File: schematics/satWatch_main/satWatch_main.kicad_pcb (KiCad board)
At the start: 2 copper layers, 40 x 30 mm, 117 parts, among them J1 PogoPins_02x17_Data, J2 UJ20-C-H-G-MSMT-2B-P16-TR, J5 Pogo_02x03_Power, Q1 FS8205, Q2 BSS138, Q3 DMP1045U, Q4 BSS138, SW1 B3U-1000P, SW2 B3U-1000P, SW3 B3U-1000P, SW4 B3U-1000P, SW5 B3U-1000P, U1 ESP32-S3-MINI-1, U10 VEMD8080, U11 VEMD8080, U12 BNO085, U2 MAX86141, U3 MAX32664GTGC, U4 NCP186AMX330TAG, U5 DS3231MZ, U6 MIC5365-1.8YC5, U7 PAM2401SCADJ, U8 TP4056-42-ESOP8, U9 DW01A, Y1 32.768kHz, Y2 32.768Hz

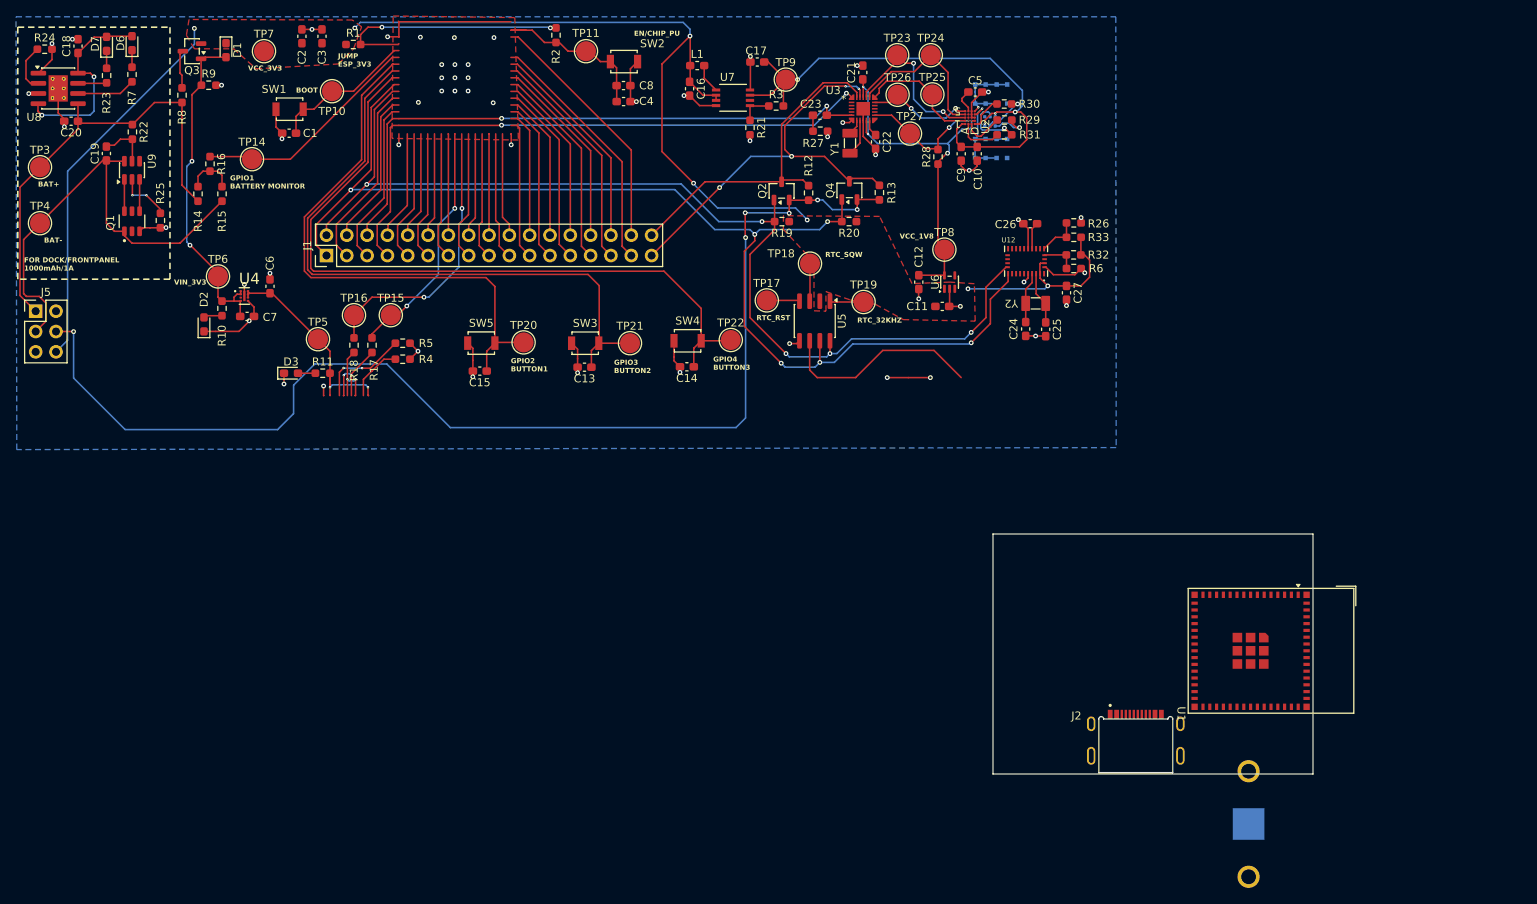
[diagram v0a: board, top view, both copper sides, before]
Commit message: v0.6
Began  layout work on watch-sized PCB. Backup of in-progress
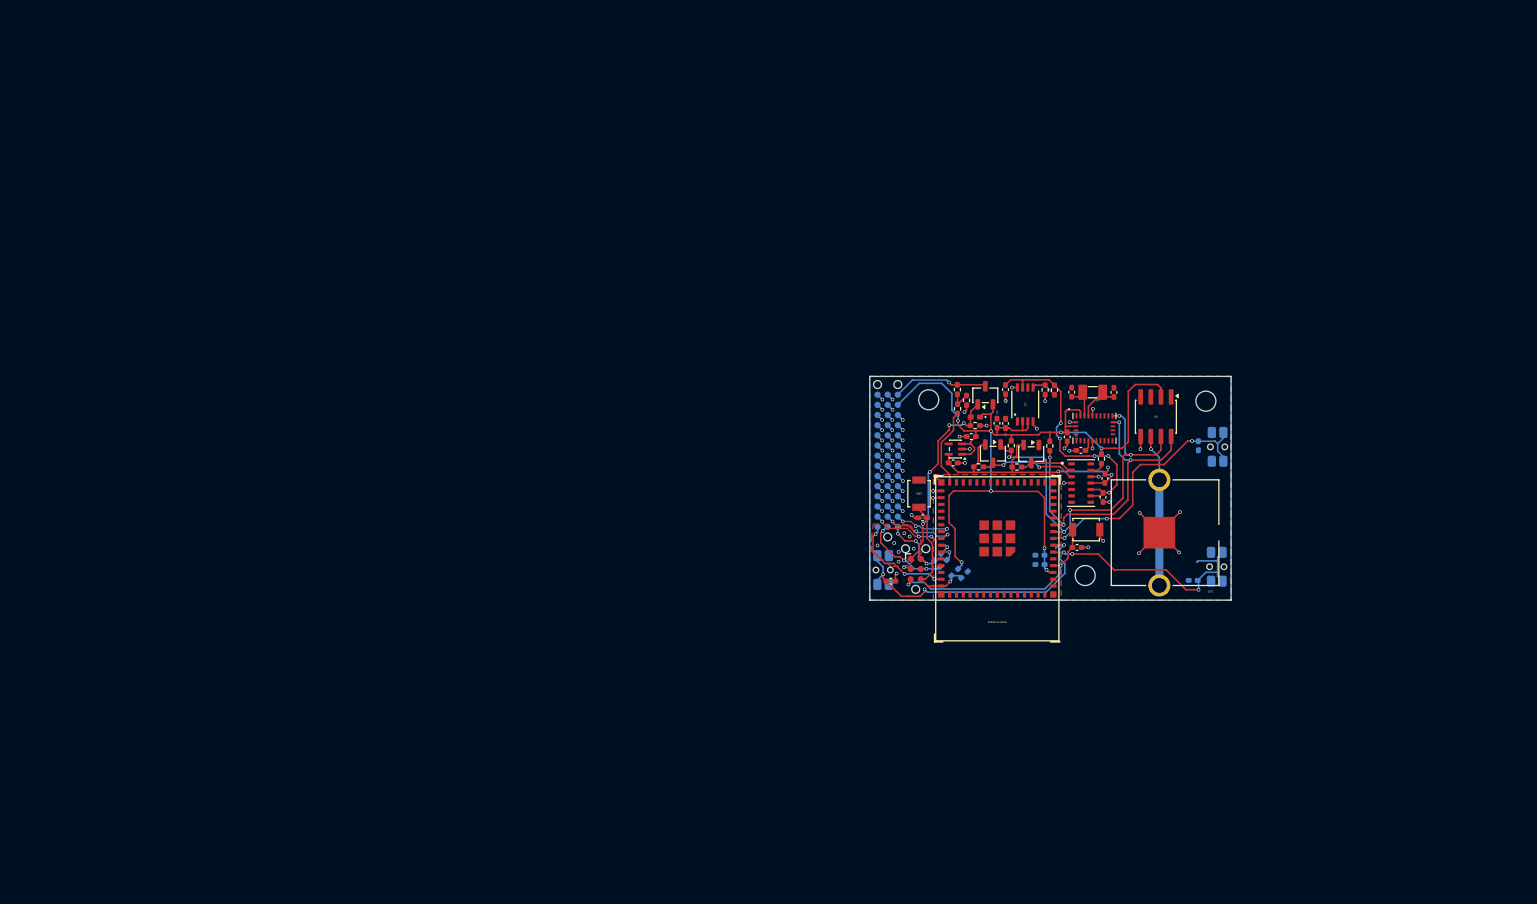
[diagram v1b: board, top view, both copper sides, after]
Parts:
- removed BT3: 2895 (CR1220 Holder), footprint:BAT_2895
- removed C19, C26, C27: 0.1uF, Capacitor_SMD:C_0603_1608Metric_Pad1.08x0.95mm_HandSolder
- removed C20: 10uF, Capacitor_SMD:C_0603_1608Metric_Pad1.08x0.95mm_HandSolder
- removed C21, C22, C23: 1uF, Capacitor_SMD:C_0603_1608Metric_Pad1.08x0.95mm_HandSolder
- removed C24, C25: 22pF, Capacitor_SMD:C_0603_1608Metric_Pad1.08x0.95mm_HandSolder
- removed D2: RED, LED_SMD:LED_0603_1608Metric_Pad1.05x0.95mm_HandSolder
- removed D3: YELLOW, LED_SMD:LED_0603_1608Metric_Pad1.05x0.95mm_HandSolder
- removed D6: DONE, LED_SMD:LED_0603_1608Metric_Pad1.05x0.95mm_HandSolder
- removed D7: CHRG, LED_SMD:LED_0603_1608Metric_Pad1.05x0.95mm_HandSolder
- removed J5: Pogo_02x03_Power, Connector_PinHeader_2.54mm:PinHeader_2x03_P2.54mm_Vertical
- removed LED1: SFH 7016, footprint:SFH7016
- removed Q4: BSS138, Package_TO_SOT_SMD:SOT-23-3
- removed R15: 220K, Resistor_SMD:R_0603_1608Metric_Pad0.98x0.95mm_HandSolder
- removed R16, R29, R30, R31, R32, R33: 0, Resistor_SMD:R_0603_1608Metric_Pad0.98x0.95mm_HandSolder
- removed R17, R18: 22, Resistor_SMD:R_0603_1608Metric_Pad0.98x0.95mm_HandSolder
- removed R19, R20: 2.2K, Resistor_SMD:R_0603_1608Metric_Pad0.98x0.95mm_HandSolder
- removed R21, R28: 100K, Resistor_SMD:R_0603_1608Metric_Pad0.98x0.95mm_HandSolder
- removed R22: 100, Resistor_SMD:R_0603_1608Metric_Pad0.98x0.95mm_HandSolder
- removed R23, R25: 1K, Resistor_SMD:R_0603_1608Metric_Pad0.98x0.95mm_HandSolder
- removed R24: 1.2k, Resistor_SMD:R_0603_1608Metric_Pad0.98x0.95mm_HandSolder
- removed R26: 10K, Resistor_SMD:R_0603_1608Metric_Pad0.98x0.95mm_HandSolder
- removed R27: 10, Resistor_SMD:R_0603_1608Metric_Pad0.98x0.95mm_HandSolder
- removed TP10: BOOT, TestPoint:TestPoint_Pad_D2.5mm
- removed TP11: EN, TestPoint:TestPoint_Pad_D2.5mm
- removed TP14: BAT_MONITOR, TestPoint:TestPoint_Pad_D2.5mm
- removed TP15: D-, TestPoint:TestPoint_Pad_D2.5mm
- removed TP16: D+, TestPoint:TestPoint_Pad_D2.5mm
- removed TP17: RTC_RST, TestPoint:TestPoint_Pad_D2.5mm
- removed TP18: SQW, TestPoint:TestPoint_Pad_D2.5mm
- removed TP19: 32KHZ, TestPoint:TestPoint_Pad_D2.5mm
- removed TP20: BUTTON1, TestPoint:TestPoint_Pad_D2.5mm
- removed TP21: BUTTON2, TestPoint:TestPoint_Pad_D2.5mm
- removed TP22: BUTTON3, TestPoint:TestPoint_Pad_D2.5mm
- removed TP23: PPG_MISO, TestPoint:TestPoint_Pad_D2.5mm
- removed TP24: PPG_MOSI, TestPoint:TestPoint_Pad_D2.5mm
- removed TP25: PPG_SCK, TestPoint:TestPoint_Pad_D2.5mm
- removed TP26: PPG_CSB, TestPoint:TestPoint_Pad_D2.5mm
- removed TP27: PPG_INT, TestPoint:TestPoint_Pad_D2.5mm
- removed TP3: BAT+, TestPoint:TestPoint_Pad_D2.5mm
- removed TP4: BAT-, TestPoint:TestPoint_Pad_D2.5mm
- removed TP5: VUSB_5V, TestPoint:TestPoint_Pad_D2.5mm
- removed TP6: VIN_3V3, TestPoint:TestPoint_Pad_D2.5mm
- removed TP7: VCC_3V3, TestPoint:TestPoint_Pad_D2.5mm
- removed TP8: VCC_1V8, TestPoint:TestPoint_Pad_D2.5mm
- removed TP9: IC_5V, TestPoint:TestPoint_Pad_D2.5mm
- removed U10, U11: VEMD8080, footprint:VEMD8080
- removed U12: BNO085, footprint:IC_BNO085
- removed U7: PAM2401SCADJ, footprint:MSOP8_DIO
- removed U8: TP4056-42-ESOP8, Package_SO:SOIC-8-1EP_3.9x4.9mm_P1.27mm_EP2.41x3.3mm_ThermalVias
- removed U9: DW01A, Package_TO_SOT_SMD:SOT-23-6
- removed Y2: 32.768Hz, footprint:ABS07-32.768KHZ-T
- added BT1: 2895 (CR1220 Holder), footprint:BAT_2895, F.Cu at (163.2, 95.7)
- added H1: MountingHole, MountingHole:MountingHole_2.5mm, F.Cu at (134.4, 79.1)
- added H2: MountingHole, MountingHole:MountingHole_2.5mm, F.Cu at (169.0, 79.3)
- added H3: MountingHole, MountingHole:MountingHole_2.5mm, F.Cu at (153.9, 101.1)
- C1: value 0.1uF/50V(10%) -> 1uF; footprint Capacitor_SMD:C_0603_1608Metric_Pad1.08x0.95mm_HandSolder -> Capacitor_SMD:C_0402_1005Metric_Pad0.74x0.62mm_HandSolder
- C10: value 0.1uF -> 10uF; footprint Capacitor_SMD:C_0603_1608Metric_Pad1.08x0.95mm_HandSolder -> Capacitor_SMD:C_0402_1005Metric_Pad0.74x0.62mm_HandSolder
- C11: value 1uF -> 0.1uF/50V(10%); footprint Capacitor_SMD:C_0603_1608Metric_Pad1.08x0.95mm_HandSolder -> Capacitor_SMD:C_0402_1005Metric_Pad0.74x0.62mm_HandSolder; moved to B.Cu
- C12, C5: value 1uF -> 0.1uF/50V(10%); footprint Capacitor_SMD:C_0603_1608Metric_Pad1.08x0.95mm_HandSolder -> Capacitor_SMD:C_0402_1005Metric_Pad0.74x0.62mm_HandSolder
- C13, C15: value 0.1uF/50V(10%) -> 0.1uF; footprint Capacitor_SMD:C_0603_1608Metric_Pad1.08x0.95mm_HandSolder -> Capacitor_SMD:C_0402_1005Metric_Pad0.74x0.62mm_HandSolder
- C14: footprint Capacitor_SMD:C_0603_1608Metric_Pad1.08x0.95mm_HandSolder -> Capacitor_SMD:C_0402_1005Metric_Pad0.74x0.62mm_HandSolder; moved to B.Cu
- C16: value 10uF -> 0.1uF; footprint Capacitor_SMD:C_0603_1608Metric_Pad1.08x0.95mm_HandSolder -> Capacitor_SMD:C_0402_1005Metric_Pad0.74x0.62mm_HandSolder
- C17: value 22uF -> 22pF; footprint Capacitor_SMD:C_0603_1608Metric_Pad1.08x0.95mm_HandSolder -> Capacitor_SMD:C_0402_1005Metric_Pad0.74x0.62mm_HandSolder
- C18: value 0.1uF -> 22pF; footprint Capacitor_SMD:C_0603_1608Metric_Pad1.08x0.95mm_HandSolder -> Capacitor_SMD:C_0402_1005Metric_Pad0.74x0.62mm_HandSolder
- C2: value 1uF/16V(10%) -> 10uF; footprint Capacitor_SMD:C_0603_1608Metric_Pad1.08x0.95mm_HandSolder -> Capacitor_SMD:C_0402_1005Metric_Pad0.74x0.62mm_HandSolder
- C3: value 10uF/16V(10%) -> 0.1uF/50V(10%); footprint Capacitor_SMD:C_0603_1608Metric_Pad1.08x0.95mm_HandSolder -> Capacitor_SMD:C_0402_1005Metric_Pad0.74x0.62mm_HandSolder
- C4: value 1uF/16V(10%) -> 1uF; footprint Capacitor_SMD:C_0603_1608Metric_Pad1.08x0.95mm_HandSolder -> Capacitor_SMD:C_0402_1005Metric_Pad0.74x0.62mm_HandSolder
- C6: value 1uF -> 22uF; footprint Capacitor_SMD:C_0603_1608Metric_Pad1.08x0.95mm_HandSolder -> Capacitor_SMD:C_0402_1005Metric_Pad0.74x0.62mm_HandSolder
- C7: value 1uF -> 1uF/16V(10%); footprint Capacitor_SMD:C_0603_1608Metric_Pad1.08x0.95mm_HandSolder -> Capacitor_SMD:C_0402_1005Metric_Pad0.74x0.62mm_HandSolder; moved to B.Cu
- C8: value 0.1uF/50V(10%) -> 1uF/16V(10%); footprint Capacitor_SMD:C_0603_1608Metric_Pad1.08x0.95mm_HandSolder -> Capacitor_SMD:C_0402_1005Metric_Pad0.74x0.62mm_HandSolder; moved to B.Cu
- C9: value 10uF -> 10uF/16V(10%); footprint Capacitor_SMD:C_0603_1608Metric_Pad1.08x0.95mm_HandSolder -> Capacitor_SMD:C_0402_1005Metric_Pad0.74x0.62mm_HandSolder; moved to B.Cu
- D1: footprint Diode_SMD:D_0603_1608Metric_Pad1.05x0.95mm_HandSolder -> Diode_SMD:D_0402_1005Metric_Pad0.77x0.64mm_HandSolder
- J1: value PogoPins_02x17_Data -> POGO_03x14; footprint Connector_PinHeader_2.54mm:PinHeader_2x17_P2.54mm_Vertical -> footprint:CUSTOM_POGO_02X21; moved to B.Cu
- J2: value UJ20-C-H-G-MSMT-2B-P16-TR -> Pogo_02x03_UARTPROG; footprint footprint:SAMESKY_UJ20-C-H-G-MSMT-2B-P16-TR -> footprint:CUSTOM_POGO_02X03
- L1: footprint Inductor_SMD:L_0603_1608Metric_Pad1.05x0.95mm_HandSolder -> Inductor_SMD:L_0402_1005Metric_Pad0.77x0.64mm_HandSolder
- Q1: value FS8205 -> DMP1045U; footprint footprint:SOT95P280X145-6N -> Package_TO_SOT_SMD:SOT-23-3
- Q3: value DMP1045U -> BSS138
- R1: value 0 -> 10K; footprint Resistor_SMD:R_0603_1608Metric_Pad0.98x0.95mm_HandSolder -> Resistor_SMD:R_0402_1005Metric_Pad0.72x0.64mm_HandSolder
- R10: value 5.1K(1%) -> 220K; footprint Resistor_SMD:R_0603_1608Metric_Pad0.98x0.95mm_HandSolder -> Resistor_SMD:R_0402_1005Metric_Pad0.72x0.64mm_HandSolder
- R11: value 5.1K(1%) -> 2.2K; footprint Resistor_SMD:R_0603_1608Metric_Pad0.98x0.95mm_HandSolder -> Resistor_SMD:R_0402_1005Metric_Pad0.72x0.64mm_HandSolder
- R12: value 2.2K -> 4.7K; footprint Resistor_SMD:R_0603_1608Metric_Pad0.98x0.95mm_HandSolder -> Resistor_SMD:R_0402_1005Metric_Pad0.72x0.64mm_HandSolder
- R13: value 2.2K -> 0; footprint Resistor_SMD:R_0603_1608Metric_Pad0.98x0.95mm_HandSolder -> Resistor_SMD:R_0402_1005Metric_Pad0.72x0.64mm_HandSolder; moved to B.Cu
- R14: value 220K -> 0; footprint Resistor_SMD:R_0603_1608Metric_Pad0.98x0.95mm_HandSolder -> Resistor_SMD:R_0402_1005Metric_Pad0.72x0.64mm_HandSolder; moved to B.Cu
- R2: value 10K(1%) -> 100K; footprint Resistor_SMD:R_0603_1608Metric_Pad0.98x0.95mm_HandSolder -> Resistor_SMD:R_0402_1005Metric_Pad0.72x0.64mm_HandSolder
- R3: footprint Resistor_SMD:R_0603_1608Metric_Pad0.98x0.95mm_HandSolder -> Resistor_SMD:R_0402_1005Metric_Pad0.72x0.64mm_HandSolder
- R4: value 5K -> 2.2K; footprint Resistor_SMD:R_0603_1608Metric_Pad0.98x0.95mm_HandSolder -> Resistor_SMD:R_0402_1005Metric_Pad0.72x0.64mm_HandSolder
- R5: value 5K -> 10K(1%); footprint Resistor_SMD:R_0603_1608Metric_Pad0.98x0.95mm_HandSolder -> Resistor_SMD:R_0402_1005Metric_Pad0.72x0.64mm_HandSolder; moved to B.Cu
- R6, R9: value 10K -> 2.2K; footprint Resistor_SMD:R_0603_1608Metric_Pad0.98x0.95mm_HandSolder -> Resistor_SMD:R_0402_1005Metric_Pad0.72x0.64mm_HandSolder
- R7: value 1K -> 0; footprint Resistor_SMD:R_0603_1608Metric_Pad0.98x0.95mm_HandSolder -> Resistor_SMD:R_0402_1005Metric_Pad0.72x0.64mm_HandSolder
- R8: value 0 -> 220K; footprint Resistor_SMD:R_0603_1608Metric_Pad0.98x0.95mm_HandSolder -> Resistor_SMD:R_0402_1005Metric_Pad0.72x0.64mm_HandSolder
- SW3, SW4, SW5: value B3U-1000P -> EVQ-P7C01P; footprint Button_Switch_SMD:SW_SPST_B3U-1000P -> Button_Switch_SMD:SW_SPST_EVQP7C; moved to B.Cu
- U1: value ESP32-S3-MINI-1 -> PAM2401SCADJ; footprint RF_Module:ESP32-S2-MINI-1 -> footprint:MSOP8_DIO
- U2: value MAX86141 -> MIC5365-1.8YC5; footprint footprint:MAX86141ENP -> Package_TO_SOT_SMD:SOT-353_SC-70-5
- U3: value MAX32664GTGC -> ESP32-S3-MINI-1; footprint footprint:MAX32664GTGB+T -> footprint:ESP32-S3-MINI-1
- U4: value NCP186AMX330TAG -> MAX30101EFD_T; footprint footprint:PSON40P160X120X45-9N -> footprint:MAX30101EFD+T
- U5: value DS3231MZ -> BNO085; footprint Package_SO:SOIC-8_3.9x4.9mm_P1.27mm -> footprint:IC_BNO085
- U6: value MIC5365-1.8YC5 -> DS3231MZ; footprint Package_TO_SOT_SMD:SOT-353_SC-70-5 -> Package_SO:SOIC-8_3.9x4.9mm_P1.27mm
- Y1: value 32.768kHz -> 32.768Hz
- moved C18 131.5 mm to (152.2, 78.2)
- moved C3 114.0 mm to (152.9, 97.6), turned to 0 degrees
- moved SW1 112.6 mm to (154.0, 95.4), turned to 180 degrees
- moved Q3 112.0 mm to (142.4, 85.9), turned to -90 degrees
- moved R7 111.3 mm to (138.0, 80.3), turned to 90 degrees
- moved Q1 108.9 mm to (141.4, 78.6)
- moved R9 107.4 mm to (140.6, 87.5)
- moved U4 107.2 mm to (153.4, 89.5)
- moved D1 104.3 mm to (140.2, 81.3), turned to 180 degrees
- moved R14 104.0 mm to (136.2, 99.6), turned to -135 degrees
- moved R8 103.7 mm to (137.9, 77.8)
- moved C2 99.4 mm to (142.9, 82.1)
- moved C7 95.3 mm to (138.8, 101.0), turned to 45 degrees
- moved R10 93.8 mm to (139.1, 79.2)
- moved C1 93.3 mm to (139.7, 83.7)
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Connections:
- C1 pad 1: /GPIO0/BOOT -> 3V3
- C10 pad 1: 5V -> GND
- C10 pad 2: GND -> 5V
- C11 pad 1: VCC_3V3 -> /GPIO2/BUTTON1
- C12 pad 1: 1V8 -> /GPIO3/BUTTON2
- C13 pad 1: /GPIO3/BUTTON2 -> 1V8
- C15 pad 1: /GPIO2/BUTTON1 -> 3V3
- C16 pad 1: VCC_3V3 -> Net-(U5-CAP)
- C17 pad 1: 5V -> Net-(U5-XOUT32/CLKSEL1)
- C18 pad 1: /VUSB_5V -> Net-(U5-XIN32)
- C2 pad 1: VCC_3V3 -> 3V3
- C3 pad 1: VCC_3V3 -> /GPIO0/BOOT
- C4 pad 1: /EN/CHIP_PU -> 1V8
- C5 pad 1: Net-(U2-VREF) -> /EN/CHIP_PU
- C6 pad 1: USB_5V -> 5V
- C7 pad 1: /VIN_3V3 -> /EN/CHIP_PU
- C8 pad 1: /EN/CHIP_PU -> 3V3
- C9 pad 1: 5V -> 3V3
- D1 pad 1: VCC_3V3 -> 3V3
- D1 pad 2: /VIN_3V3 -> VIN_3V3
- J1 pad 1: /GPIO5/SDA -> /BAT+
- J1 pad 10: /GPIO14 -> unconnected-(J1-Pin_10-Pad10)
- J1 pad 11: /GPIO15 -> /GPIO35
- J1 pad 12: /GPIO16 -> /GPIO38
- J1 pad 13: /GPIO17 -> /GPIO41
- J1 pad 14: /GPIO18 -> /U0TXD
- J1 pad 15: /GPIO21 -> unconnected-(J1-Pin_15-Pad15)
- J1 pad 16: /GPIO27 -> unconnected-(J1-Pin_16-Pad16)
- J1 pad 17: /GPIO47 -> unconnected-(J1-Pin_17-Pad17)
- J1 pad 18: /GPIO33 -> unconnected-(J1-Pin_18-Pad18)
- J1 pad 19: /GPIO34 -> unconnected-(J1-Pin_19-Pad19)
- J1 pad 2: /GPIO6/SCL -> 3V3
- J1 pad 20: /GPIO48 -> unconnected-(J1-Pin_20-Pad20)
- J1 pad 21: /GPIO35 -> unconnected-(J1-Pin_21-Pad21)
- J1 pad 22: /GPIO36 -> unconnected-(J1-Pin_22-Pad22)
- J1 pad 23: /GPIO37 -> unconnected-(J1-Pin_23-Pad23)
- J1 pad 24: /GPIO38 -> unconnected-(J1-Pin_24-Pad24)
- J1 pad 25: /GPIO39 -> /GPIO36
- J1 pad 26: /GPIO40 -> /GPIO39
- J1 pad 27: /GPIO41 -> /GPIO42
- J1 pad 28: /GPIO42 -> /U0RXD
- J1 pad 29: /U0TXD -> unconnected-(J1-Pin_29-Pad29)
- J1 pad 3: /GPIO7/SCK -> unconnected-(J1-Pin_3-Pad3)
- J1 pad 30: /U0RXD -> unconnected-(J1-Pin_30-Pad30)
- J1 pad 31: /GPIO45 -> unconnected-(J1-Pin_31-Pad31)
- J1 pad 32: /GPIO46 -> unconnected-(J1-Pin_32-Pad32)
- J1 pad 33: /LV_SDA -> unconnected-(J1-Pin_33-Pad33)
- J1 pad 34: /LV_SCL -> unconnected-(J1-Pin_34-Pad34)
- J1 pad 4: /GPIO8/MISO -> unconnected-(J1-Pin_4-Pad4)
- J1 pad 5: /GPIO9/MOSI -> unconnected-(J1-Pin_5-Pad5)
- J1 pad 6: /GPIO10 -> unconnected-(J1-Pin_6-Pad6)
- J1 pad 7: /GPIO11 -> unconnected-(J1-Pin_7-Pad7)
- J1 pad 8: /GPIO12 -> unconnected-(J1-Pin_8-Pad8)
- J1 pad 9: /GPIO13 -> unconnected-(J1-Pin_9-Pad9)
- L1 pad 1: VCC_3V3 -> 3V3
- L1 pad 2: Net-(U7-LX) -> Net-(U1-LX)
- Q1 pad 1: /BAT- -> VIN_3V3
- Q1 pad 2: unconnected-(Q1-Pad2)_1 -> 3V3
- Q1 pad 3: GND -> /BAT+
- Q2 pad 2: /VCC_1V8 -> 1V8
- Q3 pad 1: /VIN_3V3 -> /GPIO5/SDA
- Q3 pad 2: VCC_3V3 -> 1V8
- Q3 pad 3: Net-(Q3-Pad3) -> /LV_SDA
- R1 pad 1: VCC_3V3 -> VIN_3V3
- R1 pad 2: /ESP_3V3 -> GND
- R10 pad 1: /VIN_3V3 -> Net-(R10-Pad1)
- R10 pad 2: Net-(D2-A) -> GND
- R11 pad 1: Net-(D3-A) -> 3V3
- R11 pad 2: USB_5V -> /GPIO5/SDA
- R12 pad 1: /VCC_1V8 -> Net-(U4-~{INT})
- R12 pad 2: /LV_SCL -> 3V3
- R13 pad 1: /VCC_1V8 -> Net-(U3-TXD0)
- R13 pad 2: /LV_SDA -> /U0TXD
- R14 pad 1: Net-(R14-Pad1) -> Net-(U3-RXD0)
- R14 pad 2: /BAT+ -> /U0RXD
- R2 pad 1: /ESP_3V3 -> Net-(U1-FB)
- R2 pad 2: /EN/CHIP_PU -> GND
- R3 pad 1: Net-(U7-FB) -> Net-(U1-FB)
- R4 pad 1: Net-(J2-CC2) -> 1V8
- R4 pad 2: GND -> /LV_SCL
- R5 pad 1: Net-(J2-CC1) -> 3V3
- R5 pad 2: GND -> /EN/CHIP_PU
- R6 pad 1: GND -> 3V3
- R6 pad 2: /ACCEL_PS1 -> /GPIO6/SCL
- R7 pad 1: Net-(D6-K) -> /GPIO48/BATTERY_MONITOR
- R7 pad 2: Net-(U8-~{STDBY}) -> Net-(R10-Pad1)
- R8 pad 1: /BAT+ -> Net-(R10-Pad1)
- R8 pad 2: Net-(Q3-Pad3) -> /BAT+
- R9 pad 1: /VIN_3V3 -> 1V8
- R9 pad 2: GND -> /LV_SDA
- SW3 pad 2: /GPIO3/BUTTON2 -> /GPIO2/BUTTON1
- SW4 pad 2: /GPIO4/BUTTON3 -> /GPIO3/BUTTON2
- SW5 pad 2: /GPIO2/BUTTON1 -> /GPIO4/BUTTON3
- U1 pad 1: GND -> Net-(U1-LX)
- U1 pad 2: GND -> 3V3
- U1 pad 3: /ESP_3V3 -> 3V3
- U1 pad 4: /GPIO0/BOOT -> GND
- U1 pad 5: /GPIO1/BATTERY_MONITOR -> Net-(U1-FB)
- U1 pad 6: /GPIO2/BUTTON1 -> unconnected-(U1-RSET-Pad6)
- U1 pad 7: /GPIO3/BUTTON2 -> 5V
- U1 pad 8: /GPIO4/BUTTON3 -> GND
- U3 pad 1: /GPIO11 -> GND
- U3 pad 10: GND -> /GPIO6/SCL
- U3 pad 11: 1V8 -> /GPIO7/SCK
- U3 pad 12: Net-(U3-VCORE) -> /GPIO8/MISO
- U3 pad 13: unconnected-(U3-ACCEL_INT-Pad13) -> /GPIO9/MOSI
- U3 pad 14: /PPG_INT -> /GPIO10
- U3 pad 15: unconnected-(U3-NC-Pad15) -> /GPIO11
- U3 pad 16: unconnected-(U3-DNC-Pad16) -> /GPIO12
- U3 pad 17: unconnected-(U3-DNC-Pad17) -> /GPIO13
- U3 pad 18: /PPG_CSB -> /GPIO14
- U3 pad 19: /PPG_SCK -> /GPIO15
- U3 pad 2: unconnected-(U3-ACCEL_CS-Pad2) -> GND
- U3 pad 20: /PPG_MOSI -> /GPIO16
- U3 pad 21: /PPG_MISO -> /GPIO17
- U3 pad 22: 1V8 -> /GPIO18
- U3 pad 23: /LV_SDA -> /GPIO19/USBD-
- U3 pad 24: /LV_SCL -> /GPIO20/USBD+
- U3 pad 25: GND -> /GPIO21
- U3 pad 3: unconnected-(U3-NC-Pad3) -> 3V3
- U3 pad 4: unconnected-(U3-DNC-Pad4) -> /GPIO0/BOOT
- U3 pad 5: unconnected-(U3-DNC-Pad5) -> /GPIO1
- U3 pad 6: /GPIO10 -> /GPIO2/BUTTON1
- U3 pad 7: GND -> /GPIO3/BUTTON2
- U3 pad 8: Net-(U3-32KOUT) -> /GPIO4/BUTTON3
- U3 pad 9: Net-(U3-32KIN) -> /GPIO5/SDA
- U4 pad 1: /VIN_3V3 -> (no net)
- U4 pad 2: /VIN_3V3 -> /LV_SCL
- U4 pad 3: unconnected-(U4-N/C-Pad3) -> /LV_SDA
- U4 pad 4: /VIN_3V3 -> GND
- U4 pad 5: GND -> (no net)
- U4 pad 6: USB_5V -> (no net)
- U4 pad 7: USB_5V -> (no net)
- U4 pad 8: USB_5V -> (no net)
- U4 pad 9: GND -> 5V
- U5 pad 1: /32KHZ -> unconnected-(U5-RESV_NC-Pad1)
- U5 pad 2: VCC_3V3 -> GND
- U5 pad 3: /SQW -> 3V3
- U5 pad 4: /RTC_RST -> unconnected-(U5-~{BOOT}-Pad4)
- U5 pad 5: GND -> unconnected-(U5-PS1-Pad5)
- U5 pad 6: Net-(U5-VBAT) -> unconnected-(U5-PS0/WAKE-Pad6)
- U5 pad 7: /GPIO5/SDA -> unconnected-(U5-RESV_NC-Pad7)
- U5 pad 8: /GPIO6/SCL -> unconnected-(U5-RESV_NC-Pad8)
- U6 pad 1: VCC_3V3 -> unconnected-(U6-32KHZ-Pad1)
- U6 pad 2: GND -> 3V3
- U6 pad 3: VCC_3V3 -> unconnected-(U6-~{INT}/SQW-Pad3)
- U6 pad 5: 1V8 -> GND
- Y1 pad 1: Net-(U3-32KIN) -> Net-(U5-XIN32)
- Y1 pad 2: Net-(U3-32KOUT) -> Net-(U5-XOUT32/CLKSEL1)
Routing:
- net VCC_3V3: track 164.4 -> 0.00 mm, vias 7 -> 0
- net /VCC_1V8: track 149.9 -> 0.00 mm, vias 6 -> 0
- net 3V3: track 0.00 -> 114.9 mm, vias 0 -> 8
- net /GPIO5/SDA: track 150.9 -> 48.3 mm, vias 6 -> 5
- net /GPIO6/SCL: track 133.9 -> 40.0 mm, vias 5 -> 4
- net GND: track 120.6 -> 38.5 mm, vias 55 -> 36
- net /GPIO11: track 76.9 -> 0.00 mm, vias 2 -> 0
- net /GPIO10: track 75.1 -> 0.00 mm, vias 2 -> 0
- net /GPIO4/BUTTON3: track 91.2 -> 32.3 mm, vias 0 -> 3
- net /BAT-: track 56.6 -> 0.00 mm
- net /BAT+: track 57.7 -> 12.0 mm, vias 0 -> 1
- net /GPIO3/BUTTON2: track 81.8 -> 36.9 mm, vias 0 -> 3
- net /VIN_3V3: track 42.2 -> 0.00 mm, vias 2 -> 0
- net /LV_SDA: track 52.1 -> 12.3 mm, vias 4 -> 2
- net /GPIO2/BUTTON1: track 70.5 -> 31.0 mm, vias 0 -> 3
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- removed copper zone on F.Cu, net VCC_3V3
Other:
- board size 40 x 30 mm -> 45.2 x 28 mm
- copper layers 2 -> 4
- board text removed: "BAT+"
- board text removed: "BAT-"
- board text removed: "BOOT"
- board text removed: "EN/CHIP_PU"
- board text removed: "FOR DOCK/FRONTPANEL 1000mAh/1A"
- board text removed: "GPIO1 BATTERY MONITOR"
- board text removed: "GPIO2 BUTTON1"
- board text removed: "GPIO3 BUTTON2"
- board text removed: "GPIO4 BUTTON3"
- board text removed: "JUMP ESP_3V3"
- board text removed: "RTC_32KHZ"
- board text removed: "RTC_RST"
- board text removed: "RTC_SQW"
- board text removed: "VCC_1V8"
- board text removed: "VCC_3V3"
- board text removed: "VIN_3V3"

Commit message: V0.65
mainboard progress backup
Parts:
- C12: moved to B.Cu
- SW3, SW4, SW5: value EVQ-P7C01P -> EVQ-P7A01P; footprint Button_Switch_SMD:SW_SPST_EVQP7C -> Button_Switch_SMD:SW_SPST_EVQP7A
- moved SW2 11.2 mm to (129.2, 101.3), turned to 90 degrees
- moved C5 6.21 mm to (129.2, 98.2)
- moved C12 1.78 mm to (131.2, 100.9), turned to 90 degrees
- moved C11 1.75 mm to (168.7, 100.5), turned to 90 degrees
- moved C7 1.54 mm to (138.0, 102.3), turned to 0 degrees
- moved R12 1.42 mm to (157.2, 87.2), turned to 0 degrees
- moved U5 1.07 mm to (155.7, 81.8)
- moved C15 1.07 mm to (152.2, 82.9)
- moved C16 1.07 mm to (154.0, 84.5)
- moved R5 0.74 mm to (138.0, 101.3), turned to 180 degrees
- moved C17 0.67 mm to (158.1, 77.8)
- moved C18 0.67 mm to (152.8, 77.8)
- moved Y1 0.67 mm to (155.4, 77.8)
- moved SW4 0.65 mm to (128.7, 99.8)
- moved BT1 0.53 mm to (163.7, 95.7)
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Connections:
- C11 pad 1: /GPIO2/BUTTON1 -> /GPIO1/BUTTON1
- C12 pad 1: /GPIO3/BUTTON2 -> /GPIO46/BUTTON2
- C14 pad 1: /GPIO4/BUTTON3 -> /GPIO2/BUTTON3
- J1 pad 11: /GPIO35 -> /GPIO4
- J1 pad 12: /GPIO38 -> /GPIO36
- J1 pad 13: /GPIO41 -> /GPIO39
- J1 pad 25: /GPIO36 -> /GPIO3
- J1 pad 26: /GPIO39 -> /GPIO37
- J1 pad 27: /GPIO42 -> /GPIO40
- J1 pad 38: unconnected-(J1-Pin_38-Pad38) -> /GPIO2
- J1 pad 39: /GPIO37 -> /GPIO35
- J1 pad 40: /GPIO40 -> /GPIO38
- J1 pad 41: /GPIO45 -> /GPIO41
- J1 pad 42: /GPIO46 -> /GPIO42
- J2 pad 1: VIN_3V3 -> /EN/CHIP_PU
- J2 pad 2: GND -> /U0RXD
- J2 pad 3: /GPIO0/BOOT -> /U0TXD
- J2 pad 4: /EN/CHIP_PU -> VIN_3V3
- J2 pad 5: /U0RXD -> GND
- J2 pad 6: /U0TXD -> /GPIO0/BOOT
- SW3 pad 2: /GPIO2/BUTTON1 -> /GPIO1/BUTTON1
- SW4 pad 2: /GPIO3/BUTTON2 -> /GPIO46/BUTTON2
- SW5 pad 2: /GPIO4/BUTTON3 -> /GPIO2/BUTTON3
- U3 pad 44: /GPIO46 -> /GPIO46/BUTTON2
- U3 pad 5: /GPIO1 -> /GPIO1/BUTTON1
- U3 pad 6: /GPIO2/BUTTON1 -> /GPIO2/BUTTON3
- U3 pad 7: /GPIO3/BUTTON2 -> /GPIO3
- U3 pad 8: /GPIO4/BUTTON3 -> /GPIO4
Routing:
- net 3V3: track 114.9 -> 41.6 mm, vias 8 -> 12
- net /GPIO3/BUTTON2: track 36.9 -> 0.00 mm, vias 3 -> 0
- net /GPIO2/BUTTON3: track 0.00 -> 34.1 mm, vias 0 -> 3
- net /GPIO4/BUTTON3: track 32.3 -> 0.00 mm, vias 3 -> 0
- net /GPIO2/BUTTON1: track 31.0 -> 0.00 mm, vias 3 -> 0
- net /GPIO1/BUTTON1: track 0.00 -> 26.5 mm, vias 0 -> 3
- net /GPIO46: track 13.3 -> 0.00 mm, vias 3 -> 0
- net /GPIO45: track 11.5 -> 0.00 mm, vias 3 -> 0
- net /GPIO38: track 0.85 -> 9.94 mm
- net /GPIO46/BUTTON2: track 0.00 -> 8.44 mm, vias 0 -> 1
- net /GPIO35: track 1.87 -> 9.99 mm, vias 2 -> 1
- net /GPIO37: track 0.86 -> 8.54 mm
- net /GPIO40: track 0.79 -> 7.98 mm
- net /GPIO3: track 0.00 -> 6.46 mm, vias 0 -> 3
- net /GPIO2: track 0.00 -> 6.19 mm, vias 0 -> 1
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- added copper zone on B.Cu, net (none)
- added copper zone on In2.Cu, net 3V3
- added copper zone on In1.Cu, net GND
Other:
- board size 45.2 x 28 mm -> 45.7 x 28 mm
